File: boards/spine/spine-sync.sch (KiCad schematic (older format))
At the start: 24 parts, among them U7 iCE40-HX1K-TQ144

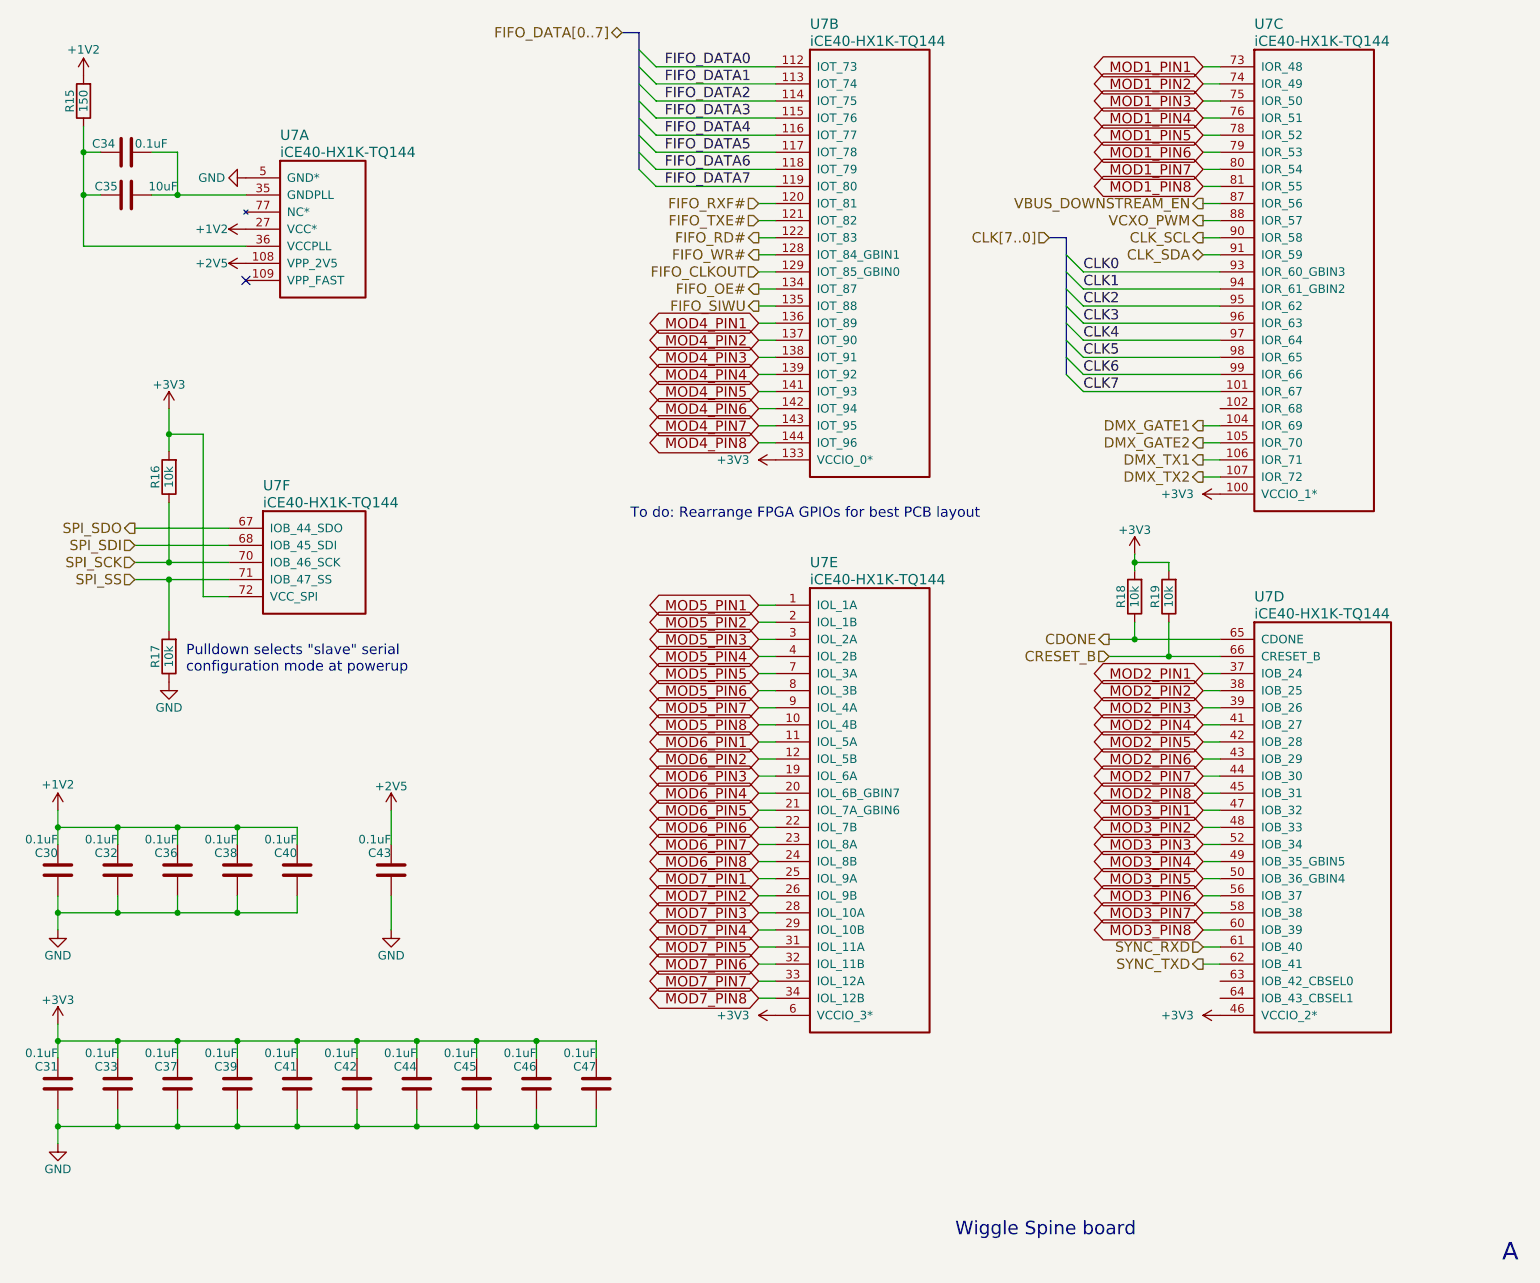
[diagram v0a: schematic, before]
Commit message: Clock generator, sync connectors, title blocks
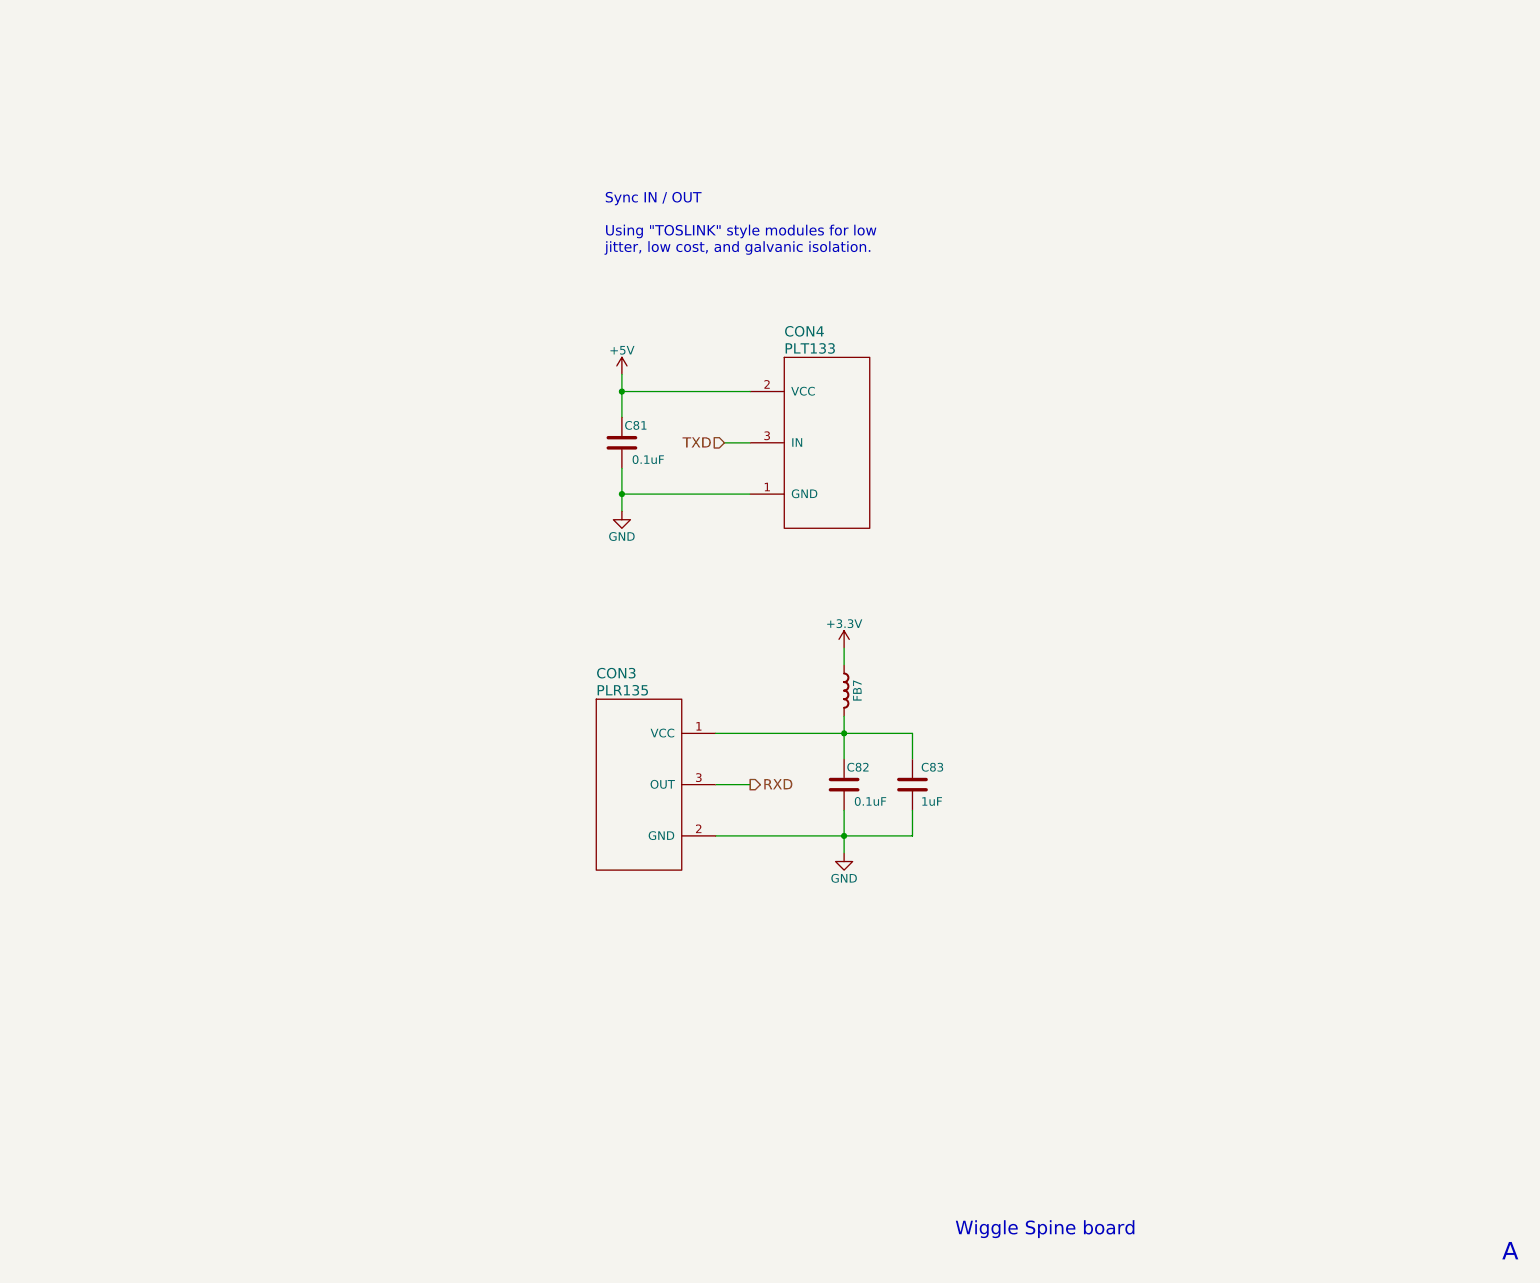
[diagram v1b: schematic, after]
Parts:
- removed C30, C31, C32, C33, C34, C36, C37, C38, C39, C40, C41, C42, C43, C44, C45, C46, C47: 0.1uF, Capacitors_SMD:C_0805, symbol C
- removed C35: 10uF, Capacitors_SMD:C_1206, symbol C
- removed R15: 150, Resistors_SMD:R_0805, symbol R
- removed R16, R17, R18, R19: 10k, Resistors_SMD:R_0805, symbol R
- removed U7: iCE40-HX1K-TQ144, symbol iCE40-HX1K-TQ144
- added C81, C82: 0.1uF, Capacitors_SMD:C_0805, symbol C
- added C83: 1uF, Capacitors_SMD:C_0805, symbol C
- added CON3: PLR135, symbol PLR135
- added CON4: PLT133, symbol PLT133/T
- added FB7: Ferrite bead, symbol FERRITE_BEAD
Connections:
- net +3V3: now also FB7.1
- net GND: now also C81.1, C82.1, C83.2, CON3.2 (GND), CON4.1 (GND)
- new net: C82.2, C83.1, CON3.1 (VCC), FB7.2
- new net +5V: C81.2, CON4.2 (VCC)
- new net RXD: CON3.3 (OUT)
- new net TXD: CON4.3 (IN)
- no-connect marks 1 -> 0
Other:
- note added: "Sync IN / OUT\n\nUsing "TOSLINK" style modules for low\njitter, low cost, and galvanic isolation."
- note removed: "Pulldown selects "slave" serial\nconfiguration mode at powerup"
- note removed: "To do: Rearrange FPGA GPIOs for best PCB layout"

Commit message: Schematic footprint and refdes work
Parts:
- CON3: footprint (none) -> TOSLINK:Everlight-PLR135-T8
- CON4: footprint (none) -> TOSLINK:Everlight-PLT133-T6A
- FB7: footprint (none) -> Resistors_SMD:R_0805
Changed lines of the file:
@@
 F 0 "CON4" H 5700 3750 60  0000 L CNN
 F 1 "PLT133" H 5700 3650 60  0000 L CNN
-F 2 "" H 5900 4000 60  0000 C CNN
+F 2 "TOSLINK:Everlight-PLT133-T6A" H 5900 4000 60  0001 C CNN
 F 3 "http://www.everlight.com/file/ProductFile/201407061806576799.pdf" H 5900 4000 60  0001 C CNN
 F 4 "Digikey" H 5900 3100 60  0001 C CNN "Vend1"
@@
 $EndComp
 $Comp
-L GND #PWR0159
+L GND #PWR160
 U 1 1 5650C9B4
 P 4750 3500
-F 0 "#PWR0159" H 4750 3250 50  0001 C CNN
+F 0 "#PWR160" H 4750 3250 50  0001 C CNN
 F 1 "GND" H 4750 3350 50  0000 C CNN
 F 2 "" H 4750 3500 60  0000 C CNN
@@
 $EndComp
 $Comp
-L +5V #PWR0160
+L +5V #PWR159
 U 1 1 5650C9FA
 P 4750 2700
-F 0 "#PWR0160" H 4750 2550 50  0001 C CNN
+F 0 "#PWR159" H 4750 2550 50  0001 C CNN
 F 1 "+5V" H 4750 2840 50  0000 C CNN
 F 2 "" H 4750 2700 60  0000 C CNN
@@
 F 0 "CON3" H 4600 5750 60  0000 L CNN
 F 1 "PLR135" H 4600 5650 60  0000 L CNN
-F 2 "" H 4800 6000 60  0000 C CNN
+F 2 "TOSLINK:Everlight-PLR135-T8" H 4800 6000 60  0001 C CNN
 F 3 "http://www.everlight.com/file/ProductFile/PLR135-T10.pdf" H 4800 6000 60  0001 C CNN
 F 4 "Digikey" H 4800 5100 60  0001 C CNN "Vend1"
@@
 $EndComp
 $Comp
-L +3.3V #PWR0161
+L +3.3V #PWR161
 U 1 1 5650E21A
 P 6050 4300
-F 0 "#PWR0161" H 6050 4150 50  0001 C CNN
+F 0 "#PWR161" H 6050 4150 50  0001 C CNN
 F 1 "+3.3V" H 6050 4440 50  0000 C CNN
 F 2 "" H 6050 4300 60  0000 C CNN
@@
 $EndComp
 $Comp
-L GND #PWR0162
+L GND #PWR162
 U 1 1 5650E275
 P 6050 5500
-F 0 "#PWR0162" H 6050 5250 50  0001 C CNN
+F 0 "#PWR162" H 6050 5250 50  0001 C CNN
 F 1 "GND" H 6050 5350 50  0000 C CNN
 F 2 "" H 6050 5500 60  0000 C CNN
@@
 F 0 "FB7" H 6200 4450 50  0000 C BNN
 F 1 "Ferrite bead" H 6450 4450 39  0001 C BNN
-F 2 "" H 6050 4550 50  0001 C CNN
+F 2 "Resistors_SMD:R_0805" H 6050 4550 50  0001 C CNN
 F 3 "http://www.samsungsem.com/kr/front/downloadcms.do?path=/kr/support/product-search/bead/__icsFiles/afieldfile/2014/11/13&fileName=S_CIB21P110NE.pdf" H 6075 4400 60  0001 C CNN
 F 4 "0.00906" H 6050 4400 60  0001 C CNN "RefPrice1k"
@@
 FB 59 00 E6 A5 69 3A 37 9E CF 73 BC F7 37 E3 33 5D 9E A8 3E 7F 80 FA F7 F6 BB 44 F4 6E D4 E7 77
 A2 1E 1F 27 A2 E3 16 70 32 E9 54 FE 3F E7 AF 00 CA 1C A3 36 0A 00 00 00 00 49 45 4E 44 AE 42 60
-82 70
+82 00
 EndData
 $EndBitmap
@@
 72 0F 1C A9 DC 70 49 CB 79 33 88 85 99 AD 01 6C 4B 10 FC 3B 13 DE 3B 37 68 79 AD 07 BC 00 3C 0E
 3C 31 EE E3 D8 E7 0F 03 D7 7B 9F FB C1 E1 FF 01 18 C4 96 1D B8 0E 40 07 00 00 00 00 49 45 4E 44
-AE 42 60 82 CA
+AE 42 60 82 00
 EndData
 $EndBitmap

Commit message: Switch to a ferrite bead with 6A current rating
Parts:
- FB7: MfgId CIB21P260NE -> CIS21P300NE; RefPrice1k 0.00906 -> 0.02383; Vend1Id 1276-6342-2-ND -> 1276-6370-1-ND
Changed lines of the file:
@@
 F 1 "Ferrite bead" H 6450 4450 39  0001 C BNN
 F 2 "Resistors_SMD:R_0805" H 6050 4550 50  0001 C CNN
-F 3 "http://www.samsungsem.com/kr/front/downloadcms.do?path=/kr/support/product-search/bead/__icsFiles/afieldfile/2014/11/13&fileName=S_CIB21P110NE.pdf" H 6075 4400 60  0001 C CNN
-F 4 "0.00906" H 6050 4400 60  0001 C CNN "RefPrice1k"
+F 3 "http://www.samsungsem.com/kr/front/downloadcms.do?path=/kr/support/product-search/bead/__icsFiles/afieldfile/2014/11/13&fileName=S_CIS21J121NE.pdf" H 6075 4400 60  0001 C CNN
+F 4 "0.02383" H 6050 4400 60  0001 C CNN "RefPrice1k"
 F 5 "Samsung" H 6050 4400 60  0001 C CNN "MfrId"
-F 6 "CIB21P260NE" H 6050 4400 60  0001 C CNN "MfgId"
+F 6 "CIS21P300NE" H 6050 4400 60  0001 C CNN "MfgId"
 F 7 "Digikey" H 6050 4400 60  0001 C CNN "Vend1"
-F 8 "1276-6342-2-ND" H 6050 4400 60  0001 C CNN "Vend1Id"
+F 8 "1276-6370-1-ND" H 6050 4400 60  0001 C CNN "Vend1Id"
 	1    6050 4400
 	0    1    1    0
